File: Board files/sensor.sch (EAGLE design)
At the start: 16 parts, among them Q1 2N3904, U1 TL974

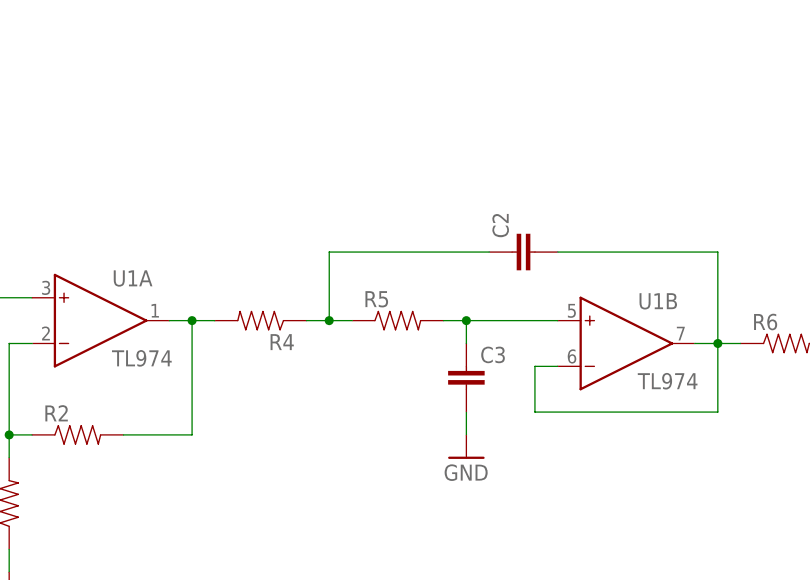
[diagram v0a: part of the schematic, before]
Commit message: Modified motor driver layout
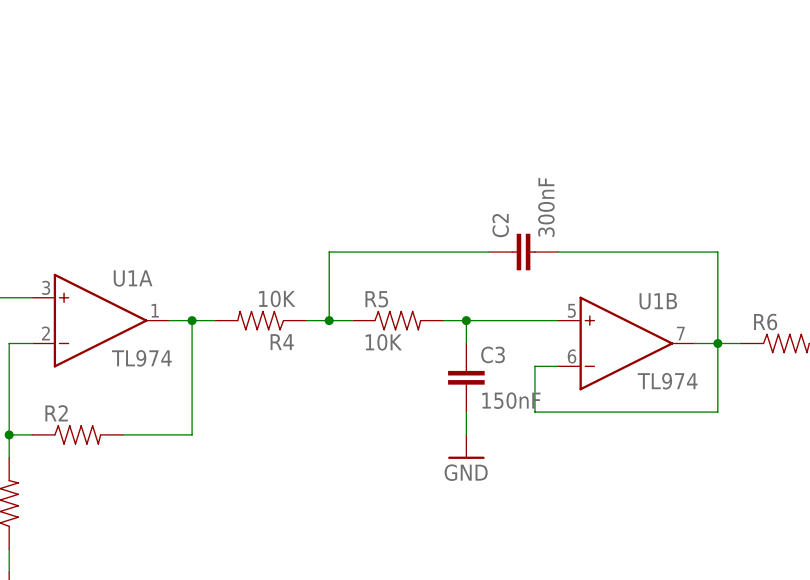
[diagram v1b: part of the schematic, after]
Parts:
- C2: value (none) -> 300nF
- C3: value (none) -> 150nF
- R4, R5: value (none) -> 10K
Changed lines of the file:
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@@
 <part name="GND5" library="SparkFun-Aesthetics" deviceset="GND" device=""/>
 <part name="GND7" library="SparkFun-Aesthetics" deviceset="GND" device=""/>
-<part name="R4" library="SparkFun-Resistors" deviceset="RESISTOR" device="0805-RES"/>
-<part name="R5" library="SparkFun-Resistors" deviceset="RESISTOR" device="0805-RES"/>
+<part name="R4" library="SparkFun-Resistors" deviceset="RESISTOR" device="0805-RES" value="10K"/>
+<part name="R5" library="SparkFun-Resistors" deviceset="RESISTOR" device="0805-RES" value="10K"/>
 <part name="R6" library="SparkFun-Resistors" deviceset="RESISTOR" device="0805-RES"/>
-<part name="C2" library="SparkFun-Capacitors" deviceset="CAP" device="0805"/>
-<part name="C3" library="SparkFun-Capacitors" deviceset="CAP" device="0805"/>
+<part name="C2" library="SparkFun-Capacitors" deviceset="CAP" device="0805" value="300nF"/>
+<part name="C3" library="SparkFun-Capacitors" deviceset="CAP" device="0805" value="150nF"/>
 <part name="Q1" library="SparkFun-DiscreteSemi" deviceset="TRANSISTOR_NPN" device="SOT23" value="2N3904"/>
 <part name="GND8" library="SparkFun-Aesthetics" deviceset="GND" device=""/>

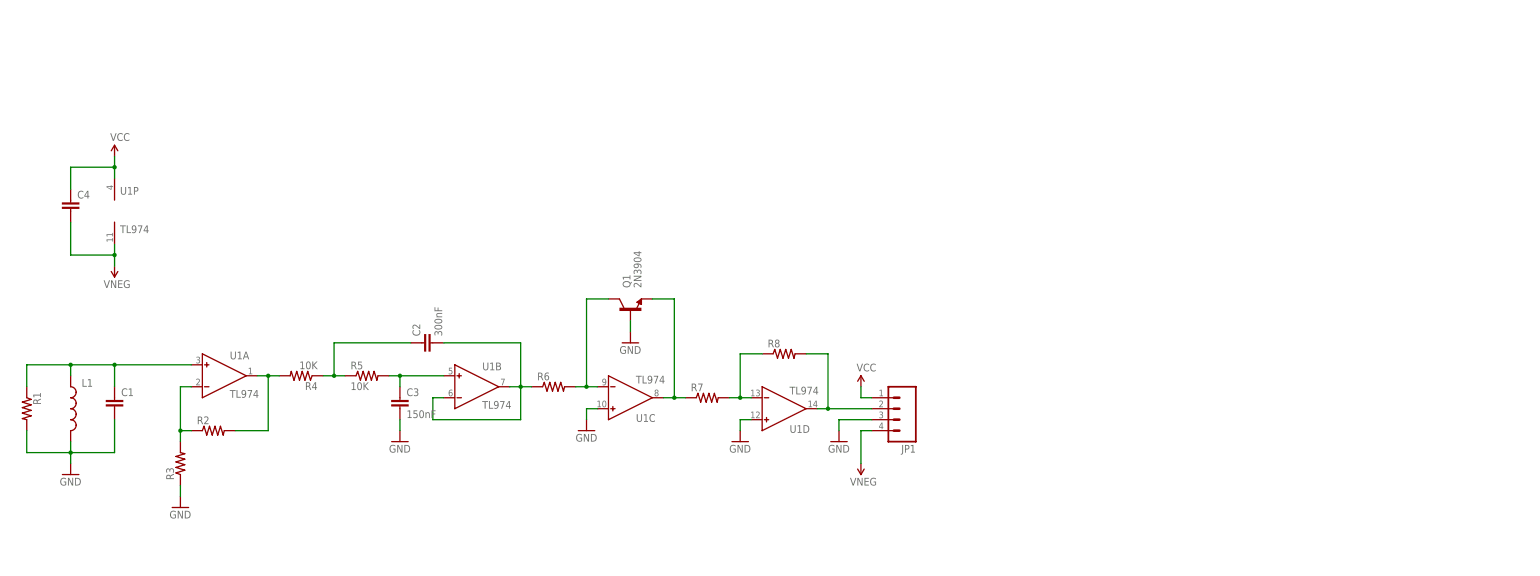
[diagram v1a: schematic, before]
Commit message: Significantly modified sensor circuit
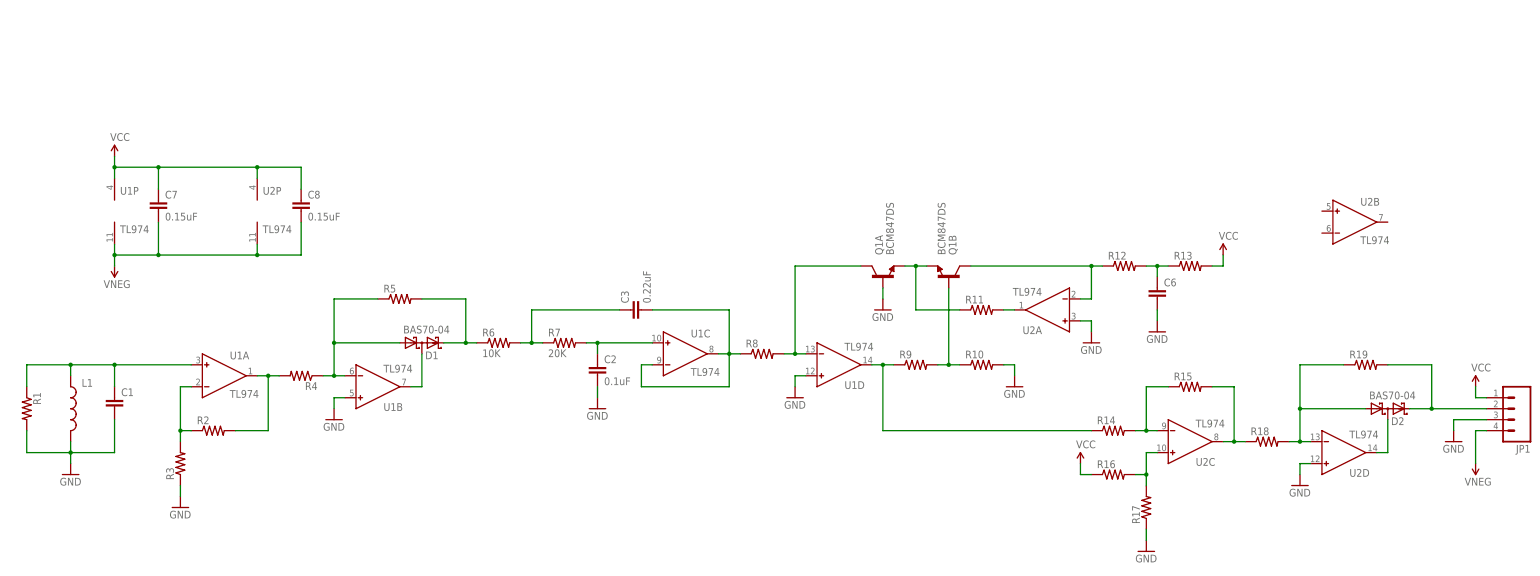
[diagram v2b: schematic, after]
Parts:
- removed C4: (no value), SparkFun-Capacitors:CAP0805
- added C6: (no value), SparkFun-Capacitors:CAP0805
- added C7, C8: 0.15uF, SparkFun-Capacitors:CAP0805
- added D1, D2: BAS70-04, diode:BAS70-04
- added R10, R11, R12, R13, R14, R15, R16, R17, R18, R19, R9: (no value), SparkFun-Resistors:RESISTOR0805-RES
- added U2: TL974, Custom:TL974
- C2: value 300nF -> 0.1uF
- C3: value 150nF -> 0.22uF
- Q1: value 2N3904 -> BCM847DS; device SparkFun-DiscreteSemi:TRANSISTOR_NPNSOT23 -> Custom:BCM847DS
- R4, R5: value 10K -> (none)
- R6: value (none) -> 10K
- R7: value (none) -> 20K
- U1: device analog-devices:AD8644R -> Custom:TL974
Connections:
- removed net N$11: JP1.2, R8.2, U1D.OUT
- removed net N$9: Q1.C, R6.2, U1C.IN-
- new net N$10: C3.2, R8.1, U1C.IN-, U1C.OUT
- new net N$13: Q1A.C, R8.2, U1D.IN-
- new net N$14: R11.2, U2A.OUT
- new net N$15: Q1A.E, Q1B.E, R11.1
- new net N$16: Q1B.B, R10.1, R9.2
- new net N$17: R14.1, R9.1, U1D.OUT
- new net N$18: C6.1, R12.2, R13.1
- new net N$19: Q1B.C, R12.1, U2A.IN-
- new net N$20: R16.2, R17.2, U2C.IN+
- new net N$22: R14.2, R15.1, U2C.IN-
- new net N$23: D2.A1, R18.2, R19.1, U2D.IN-
- new net N$24: R15.2, R18.1, U2C.OUT
- new net N$25: D2.C1A2, U2D.OUT
- new net N$26: D2.C2, JP1.2, R19.2
- net GND: now also C2.2, C6.2, Q1A.B, R10.2, R17.1, U1B.IN+, U2A.IN+, U2D.IN+; no longer C3.2, Q1.B, U1C.IN+
- net N$2: now also D1.A1, R4.1, R5.1; no longer C2.2, R6.1, U1B.OUT
- net N$5: now also D1.C2, R6.1; no longer C3.1, U1B.IN+
- net N$6: now also R7.2, U1C.IN+; no longer R4.1, R5.1
- net N$7: now also C3.1, R6.2, R7.1; no longer R7.2, R8.1, U1D.IN-
- net N$8: now also D1.C1A2, U1B.OUT; no longer Q1.E, R7.1, U1C.OUT
- net VCC: now also C7.1, C8.1, R13.2, R16.1, U2P.V+; no longer C4.1
- net VNEG: now also C7.2, C8.2, U2P.V-; no longer C4.2
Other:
- moved on the sheet: C2, C3, JP1, R5, R6, R7, R8, U1B, U1C, U1D

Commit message: Finished new sensor board layout
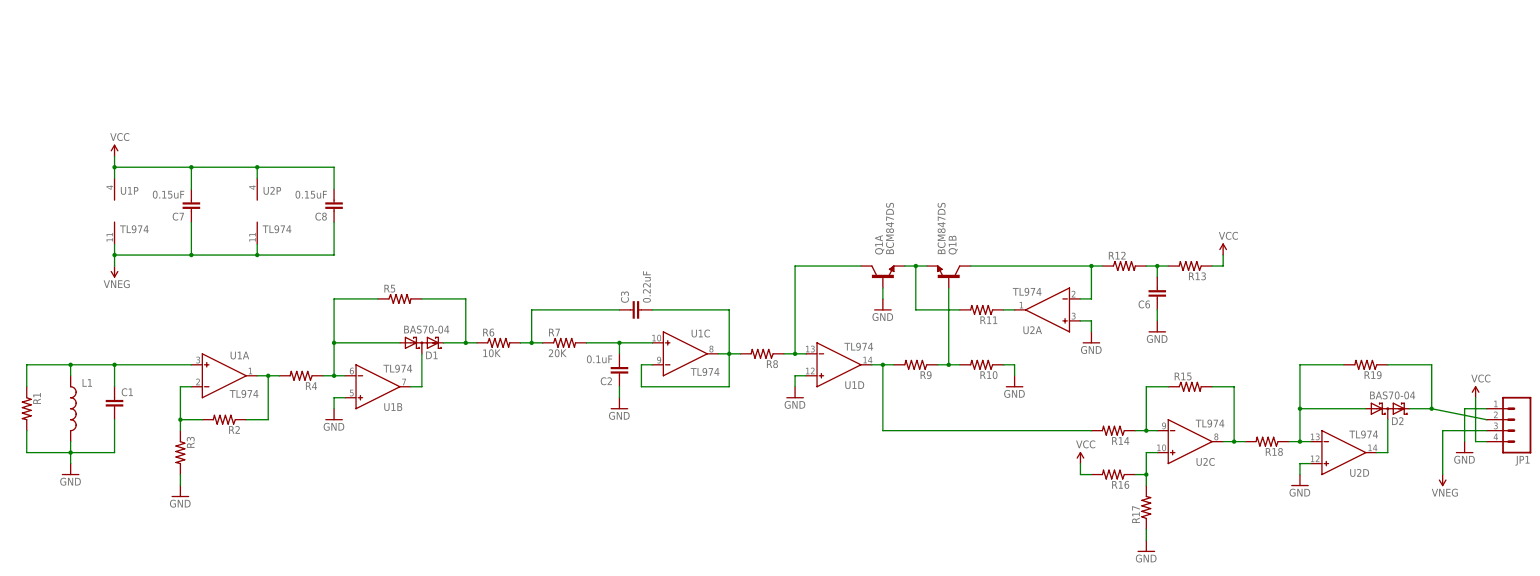
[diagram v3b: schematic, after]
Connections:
- net GND: now also C2.1, C6.1, JP1.1, R10.1, R3.2; no longer C2.2, C6.2, JP1.3, R10.2, R3.1
- net N$10: now also R8.2; no longer R8.1
- net N$13: now also R8.1; no longer R8.2
- net N$14: now also R11.1; no longer R11.2
- net N$15: now also R11.2; no longer R11.1
- net N$16: now also R10.2, R9.1; no longer R10.1, R9.2
- net N$17: now also R14.2, R9.2; no longer R14.1, R9.1
- net N$18: now also C6.2, R13.2; no longer C6.1, R13.1
- net N$20: now also R16.1; no longer R16.2
- net N$22: now also R14.1; no longer R14.2
- net N$23: now also R18.1, R19.2; no longer R18.2, R19.1
- net N$24: now also R18.2; no longer R18.1
- net N$26: now also R19.1; no longer R19.2
- net N$3: now also R2.2, R3.1; no longer R2.1, R3.2
- net N$4: now also R2.1; no longer R2.2
- net N$6: now also C2.2; no longer C2.1
- net VCC: now also C7.2, C8.2, JP1.4, R13.1, R16.2; no longer C7.1, C8.1, JP1.1, R13.2, R16.1
- net VNEG: now also C7.1, C8.1, JP1.3; no longer C7.2, C8.2, JP1.4
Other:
- moved on the sheet: C2, C6, C7, C8, JP1, R10, R11, R13, R14, R16, R18, R19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

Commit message: Added component values and removed final rectifier
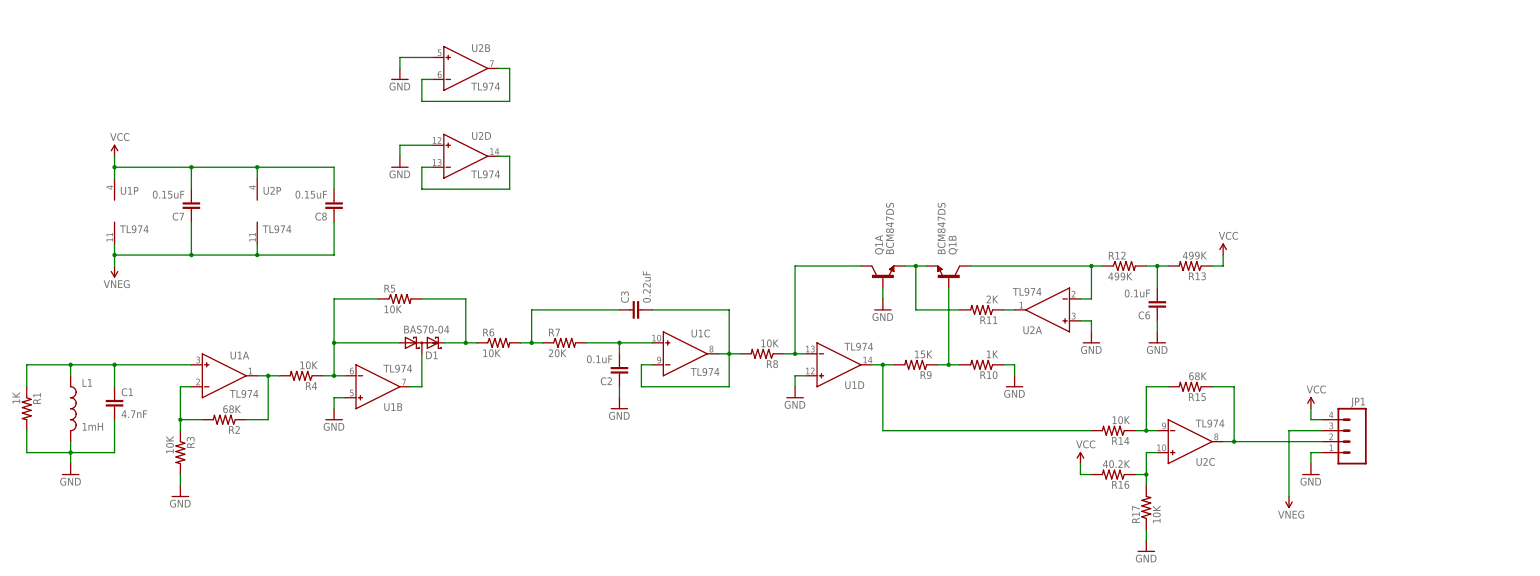
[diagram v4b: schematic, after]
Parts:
- removed D2: BAS70-04, diode:BAS70-04
- removed R18, R19: (no value), SparkFun-Resistors:RESISTOR0805-RES
- C1: value (none) -> 4.7nF
- C6: value (none) -> 0.1uF
- L1: value (none) -> 1mH
- R1, R10: value (none) -> 1K
- R11: value (none) -> 2K
- R12, R13: value (none) -> 499K
- R14, R17, R3, R4, R5, R8: value (none) -> 10K
- R15, R2: value (none) -> 68K
- R16: value (none) -> 40.2K
- R9: value (none) -> 15K
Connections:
- removed net N$23: D2.A1, R18.1, R19.2, U2D.IN-
- removed net N$25: D2.C1A2, U2D.OUT
- removed net N$26: D2.C2, JP1.2, R19.1
- new net N$11: U2D.IN-, U2D.OUT
- new net N$9: U2B.IN-, U2B.OUT
- net GND: now also U2B.IN+
- net N$22: now also R15.2; no longer R15.1
- net N$24: now also JP1.2, R15.1; no longer R15.2, R18.2
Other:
- moved on the sheet: C6, JP1, R15, U2D

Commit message: Fixed decoupling caps and added labels
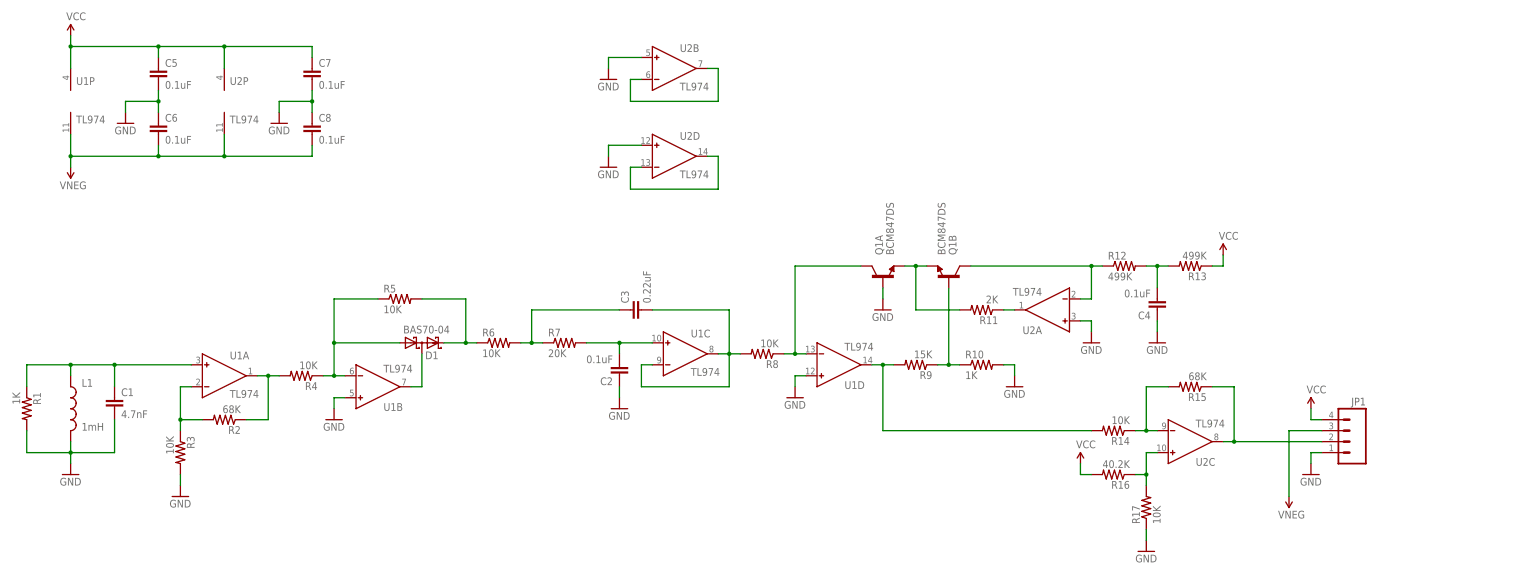
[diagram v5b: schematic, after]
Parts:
- added C4, C5: 0.1uF, SparkFun-Capacitors:CAP0805
- C7, C8: value 0.15uF -> 0.1uF
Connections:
- net GND: now also C4.1, C5.2, C7.2, C8.1, R10.2; no longer R10.1
- net N$16: now also R10.1; no longer R10.2
- net N$18: now also C4.2; no longer C6.2
- net VCC: now also C5.1, C7.1; no longer C7.2, C8.2
- net VNEG: now also C6.2, C8.2; no longer C7.1, C8.1
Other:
- moved on the sheet: C6, C7, C8, R10, U1P, U2B, U2D, U2P

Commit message: Added larger decoupling capacitors to the sensor boards
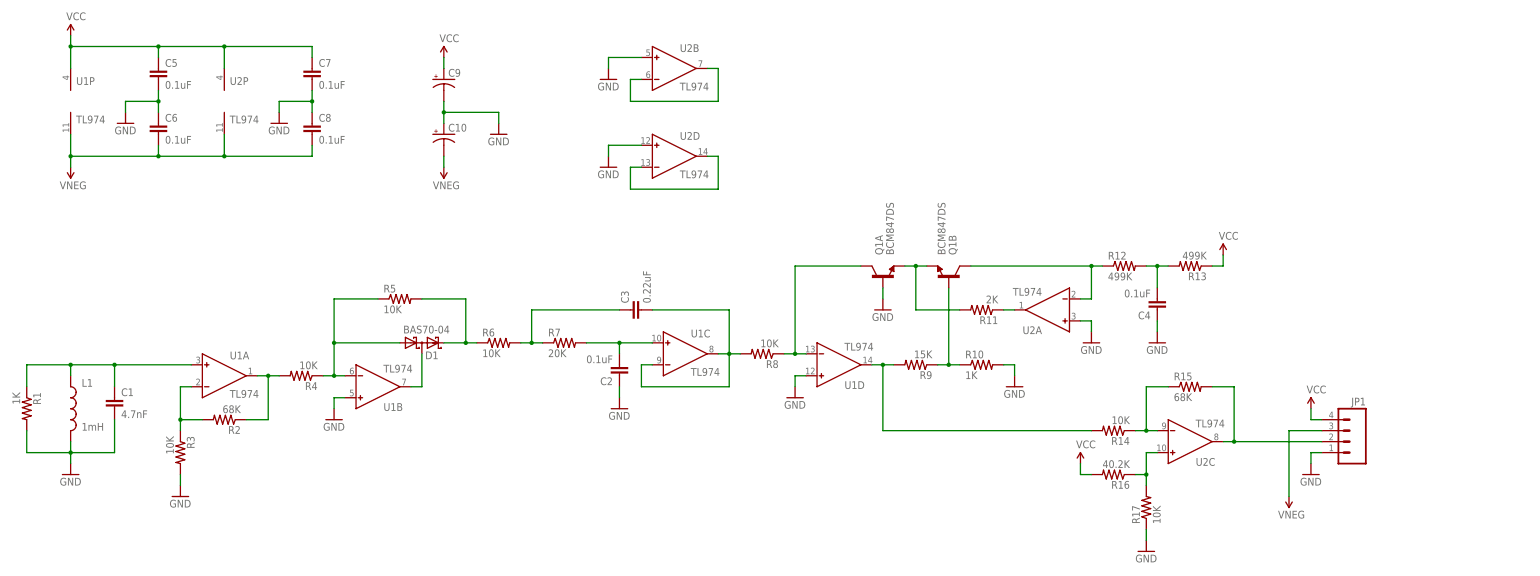
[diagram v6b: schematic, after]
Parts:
- added C10, C9: (no value), resistor:CPOL-USE2-4
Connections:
- net GND: now also C10.+, C9.-
- net N$22: now also R15.1; no longer R15.2
- net N$24: now also R15.2; no longer R15.1
- net VCC: now also C9.+
- net VNEG: now also C10.-
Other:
- moved on the sheet: R15
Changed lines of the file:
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@@
 <part name="GND14" library="SparkFun-Aesthetics" deviceset="GND" device=""/>
 <part name="GND15" library="SparkFun-Aesthetics" deviceset="GND" device=""/>
+<part name="C9" library="resistor" deviceset="CPOL-US" device="E2-4"/>
+<part name="C10" library="resistor" deviceset="CPOL-US" device="E2-4"/>
+<part name="SUPPLY7" library="SparkFun-Aesthetics" deviceset="VCC" device=""/>
+<part name="SUPPLY8" library="SparkFun-Aesthetics" deviceset="VNEG" device=""/>
+<part name="GND16" library="SparkFun-Aesthetics" deviceset="GND" device=""/>
 </parts>
 <sheets>
@@
 <instance part="GND11" gate="1" x="269.24" y="48.26"/>
 <instance part="R14" gate="G$1" x="259.08" y="27.94" rot="R180"/>
-<instance part="R15" gate="G$1" x="276.86" y="38.1" rot="R180"/>
+<instance part="R15" gate="G$1" x="276.86" y="38.1"/>
 <instance part="GND13" gate="1" x="266.7" y="0"/>
 <instance part="SUPPLY6" gate="1" x="251.46" y="20.32"/>
@@
 <instance part="GND14" gate="1" x="30.48" y="99.06"/>
 <instance part="GND15" gate="1" x="66.04" y="99.06"/>
+<instance part="C9" gate="G$1" x="104.14" y="109.22"/>
+<instance part="C10" gate="G$1" x="104.14" y="96.52"/>
+<instance part="SUPPLY7" gate="1" x="104.14" y="114.3"/>
+<instance part="SUPPLY8" gate="G$2" x="104.14" y="86.36"/>
+<instance part="GND16" gate="1" x="116.84" y="96.52"/>
 </instances>
 <busses>
@@
 <wire x1="66.04" y1="104.14" x2="66.04" y2="101.6" width="0.1524" layer="91"/>
 <junction x="73.66" y="104.14"/>
+</segment>
+<segment>
+<pinref part="C9" gate="G$1" pin="-"/>
+<pinref part="C10" gate="G$1" pin="+"/>
+<wire x1="104.14" y1="104.14" x2="104.14" y2="101.6" width="0.1524" layer="91"/>
+<pinref part="GND16" gate="1" pin="GND"/>
+<wire x1="104.14" y1="101.6" x2="104.14" y2="99.06" width="0.1524" layer="91"/>
+<wire x1="104.14" y1="101.6" x2="116.84" y2="101.6" width="0.1524" layer="91"/>
+<wire x1="116.84" y1="101.6" x2="116.84" y2="99.06" width="0.1524" layer="91"/>
+<junction x="104.14" y="101.6"/>
 </segment>
 </net>
@@
 <junction x="38.1" y="116.84"/>
 </segment>
+<segment>
+<pinref part="C9" gate="G$1" pin="+"/>
+<pinref part="SUPPLY7" gate="1" pin="VCC"/>
+<wire x1="104.14" y1="114.3" x2="104.14" y2="111.76" width="0.1524" layer="91"/>
+</segment>
 </net>
 <net name="N$3" class="0">
@@
 <junction x="38.1" y="91.44"/>
 </segment>
+<segment>
+<pinref part="C10" gate="G$1" pin="-"/>
+<pinref part="SUPPLY8" gate="G$2" pin="VNEG"/>
+<wire x1="104.14" y1="88.9" x2="104.14" y2="91.44" width="0.1524" layer="91"/>
+</segment>
 </net>
 <net name="N$2" class="0">
@@
 <pinref part="U2" gate="C" pin="IN-"/>
 <wire x1="264.16" y1="27.94" x2="266.7" y2="27.94" width="0.1524" layer="91"/>
-<pinref part="R15" gate="G$1" pin="2"/>
+<pinref part="R15" gate="G$1" pin="1"/>
 <wire x1="266.7" y1="27.94" x2="269.24" y2="27.94" width="0.1524" layer="91"/>
 <wire x1="271.78" y1="38.1" x2="266.7" y2="38.1" width="0.1524" layer="91"/>
@@
 <pinref part="U2" gate="C" pin="OUT"/>
 <wire x1="284.48" y1="25.4" x2="287.02" y2="25.4" width="0.1524" layer="91"/>
-<pinref part="R15" gate="G$1" pin="1"/>
+<pinref part="R15" gate="G$1" pin="2"/>
 <wire x1="287.02" y1="25.4" x2="287.02" y2="38.1" width="0.1524" layer="91"/>
 <wire x1="287.02" y1="38.1" x2="281.94" y2="38.1" width="0.1524" layer="91"/>
